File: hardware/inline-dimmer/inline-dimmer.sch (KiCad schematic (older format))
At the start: 15 parts, among them J1 Conn_01x01, J2 Conn_01x01, J3 1984633, J4 M5, J5 M5, Q2 DMP3013SFV, U1 MIC1555YM5-TR

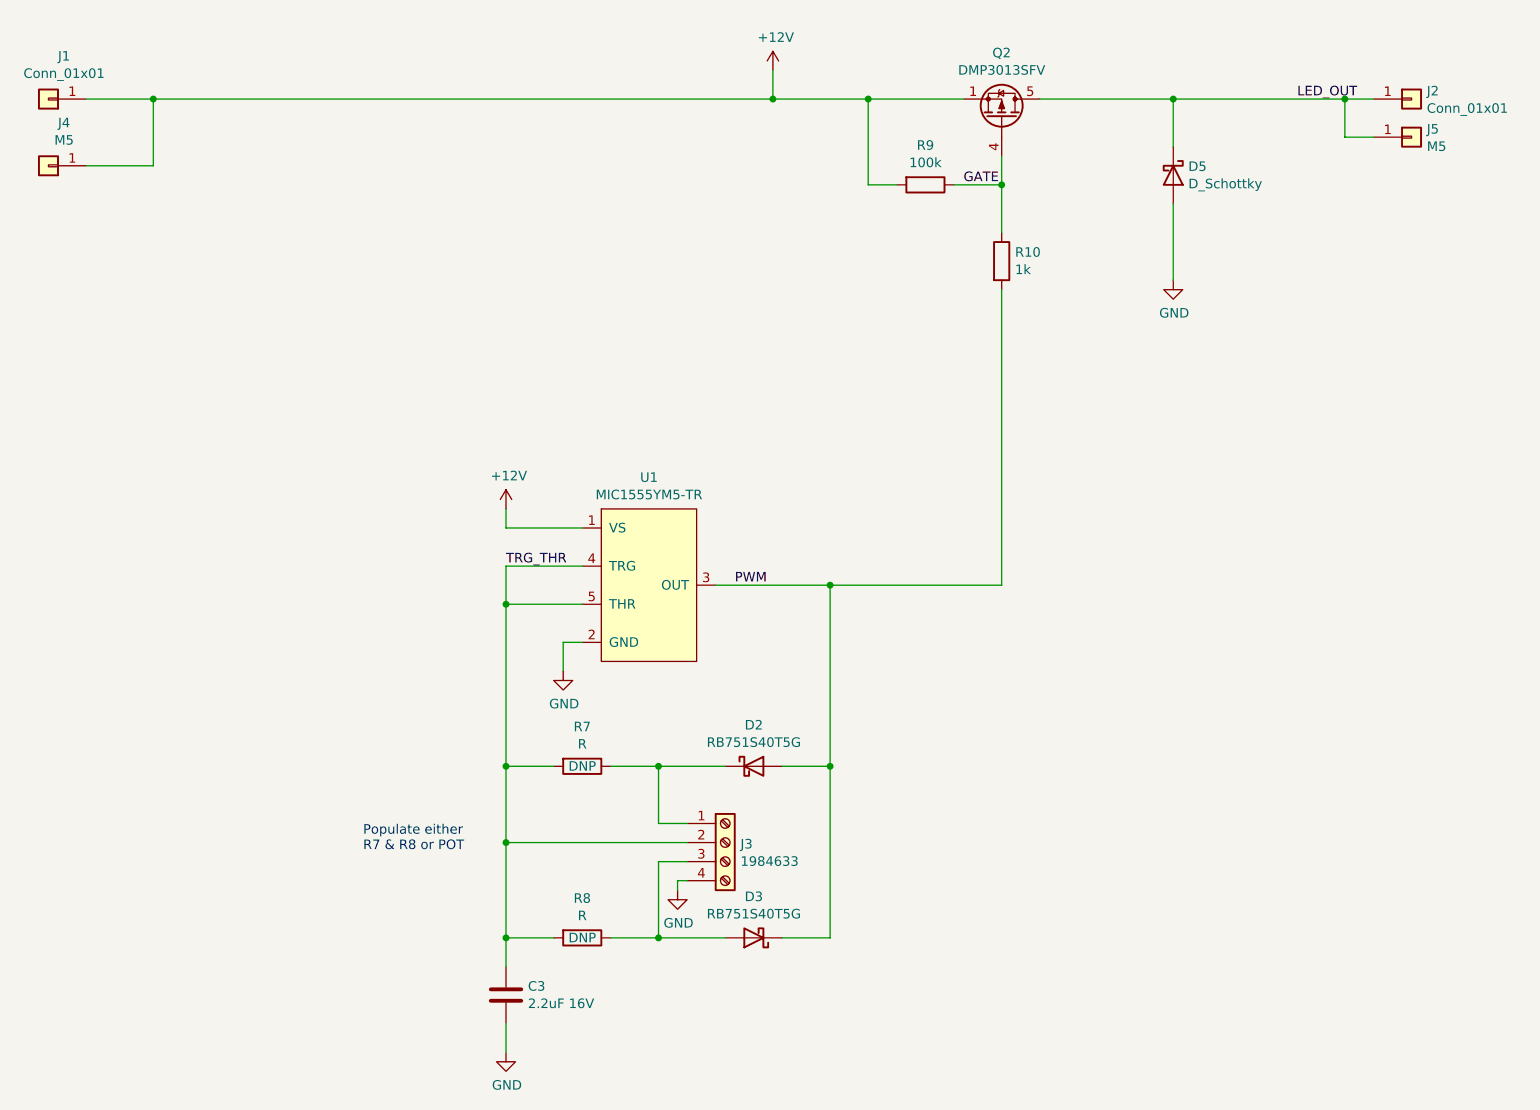
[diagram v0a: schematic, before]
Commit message: Added silkscreen and LED
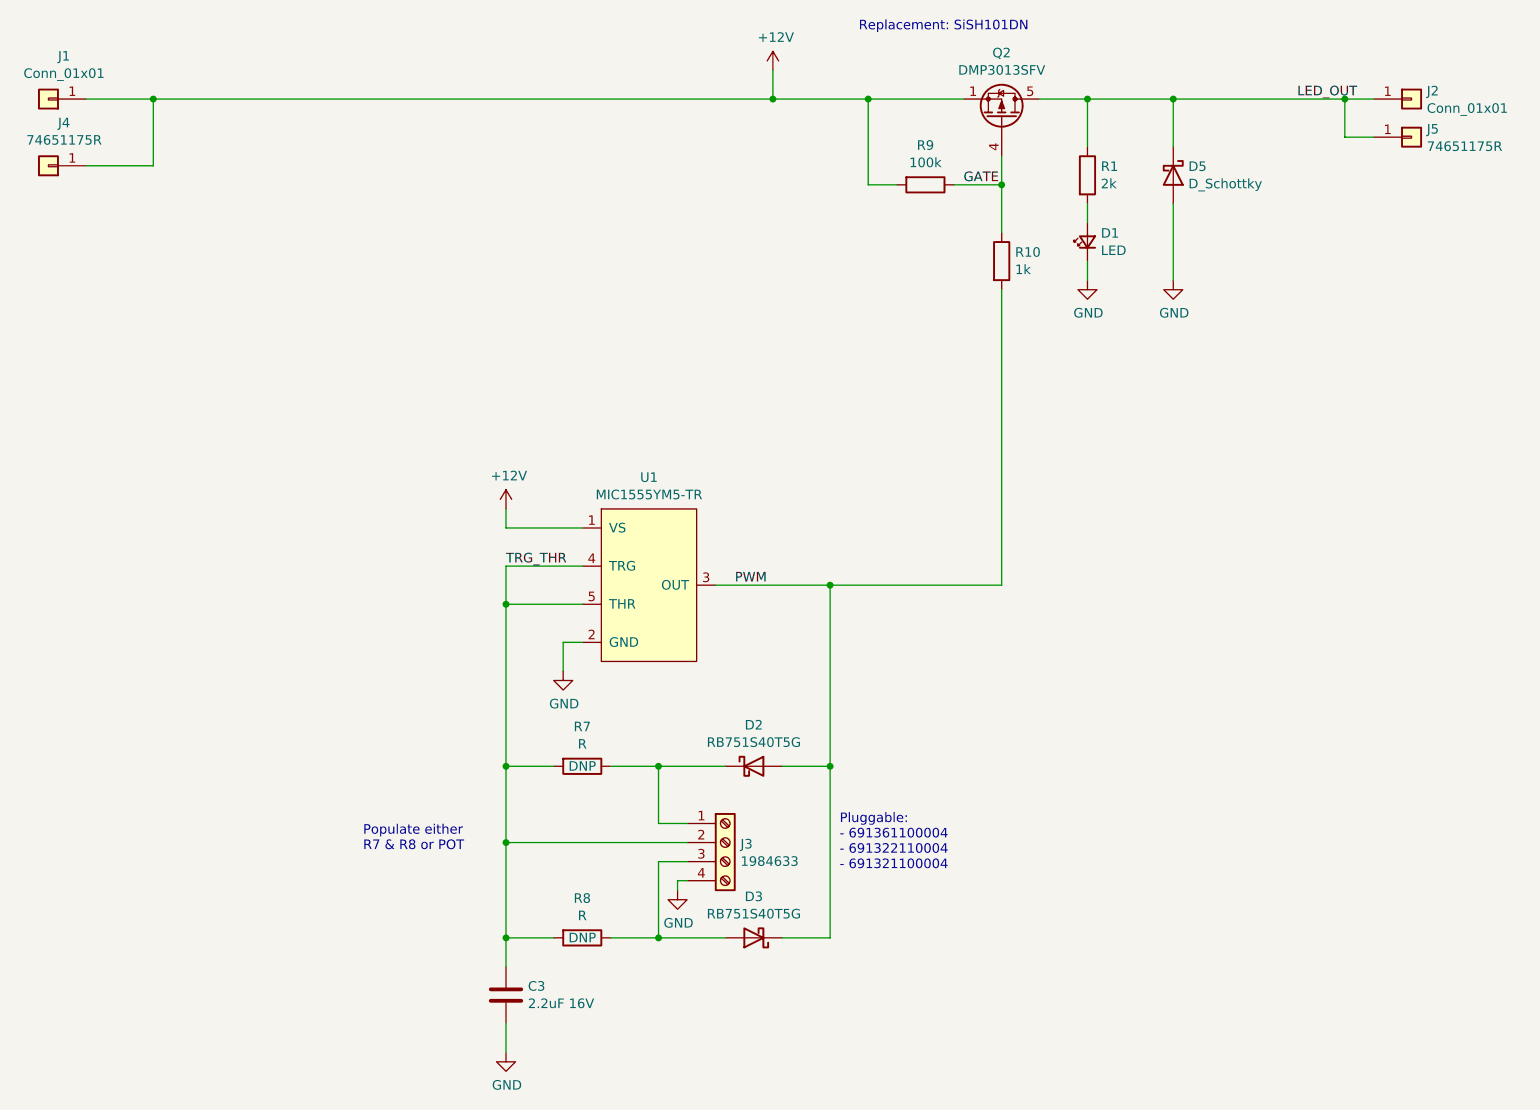
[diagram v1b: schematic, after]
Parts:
- added D1: LED, LED_SMD:LED_0603_1608Metric, symbol Device:LED_Small
- added R1: 2k, Resistor_SMD:R_0603_1608Metric, symbol Device:R
- J4, J5: value M5 -> 74651175R
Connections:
- net GND: now also D1.1 (K)
- net LED_OUT: now also R1.1
- new net: D1.2 (A), R1.2
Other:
- note added: "Pluggable:\n- 691361100004\n- 691322110004\n- 691321100004\n"
- note added: "Replacement: SiSH101DN"
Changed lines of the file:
@@
 Connection ~ 5900 1400
 Wire Wire Line
-	7300 1400 8000 1400
+	7300 1400 7550 1400
 $Comp
 L Device:R R9
@@
 P 9250 1600
 F 0 "J5" H 9330 1642 50  0000 L CNN
-F 1 "M5" H 9330 1551 50  0000 L CNN
+F 1 "74651175R" H 9330 1551 50  0000 L CNN
 F 2 "connectors:M5_74651175R_Solder" H 9250 1600 50  0001 C CNN
 F 3 "~" H 9250 1600 50  0001 C CNN
@@
 P 2100 1750
 F 0 "J4" H 2018 1525 50  0000 C CNN
-F 1 "M5" H 2018 1616 50  0000 C CNN
+F 1 "74651175R" H 2018 1616 50  0000 C CNN
 F 2 "connectors:M5_74651175R_Solder" H 2100 1750 50  0001 C CNN
 F 3 "~" H 2100 1750 50  0001 C CNN
@@
 Wire Wire Line
 	2650 1400 5900 1400
+$Comp
+L Device:R R1
+U 1 1 60A142A9
+P 7550 1800
+F 0 "R1" H 7620 1846 50  0000 L CNN
+F 1 "2k" H 7620 1755 50  0000 L CNN
+F 2 "Resistor_SMD:R_0603_1608Metric" V 7480 1800 50  0001 C CNN
+F 3 "~" H 7550 1800 50  0001 C CNN
+	1    7550 1800
+	1    0    0    -1
+$EndComp
+$Comp
+L Device:LED_Small D1
+U 1 1 60A14773
+P 7550 2150
+F 0 "D1" V 7596 2080 50  0000 R CNN
+F 1 "LED" V 7505 2080 50  0000 R CNN
+F 2 "LED_SMD:LED_0603_1608Metric" V 7550 2150 50  0001 C CNN
+F 3 "~" V 7550 2150 50  0001 C CNN
+	1    7550 2150
+	0    -1   -1   0
+$EndComp
+Wire Wire Line
+	7550 1650 7550 1400
+Connection ~ 7550 1400
+Wire Wire Line
+	7550 1400 8000 1400
+Wire Wire Line
+	7550 2050 7550 1950
+$Comp
+L power:GND #PWR0104
+U 1 1 60A17708
+P 7550 2350
+F 0 "#PWR0104" H 7550 2100 50  0001 C CNN
+F 1 "GND" H 7555 2177 50  0000 C CNN
+F 2 "" H 7550 2350 50  0001 C CNN
+F 3 "" H 7550 2350 50  0001 C CNN
+	1    7550 2350
+	1    0    0    -1
+$EndComp
+Wire Wire Line
+	7550 2350 7550 2250
+Text Notes 6250 5450 0    50   ~ 0
+Pluggable:\n- 691361100004\n- 691322110004\n- 691321100004\n
+Text Notes 6350 1050 0    50   ~ 0
+Replacement: SiSH101DN
 $EndSCHEMATC
